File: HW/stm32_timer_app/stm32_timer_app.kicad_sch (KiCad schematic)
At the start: 20 parts, among them J1 105164-0001, J2 61300411121, Q1 BTA10-600BRG, U1 RT9193-33GB, U2 MOC3041SM, U3 STM32F103C8T6

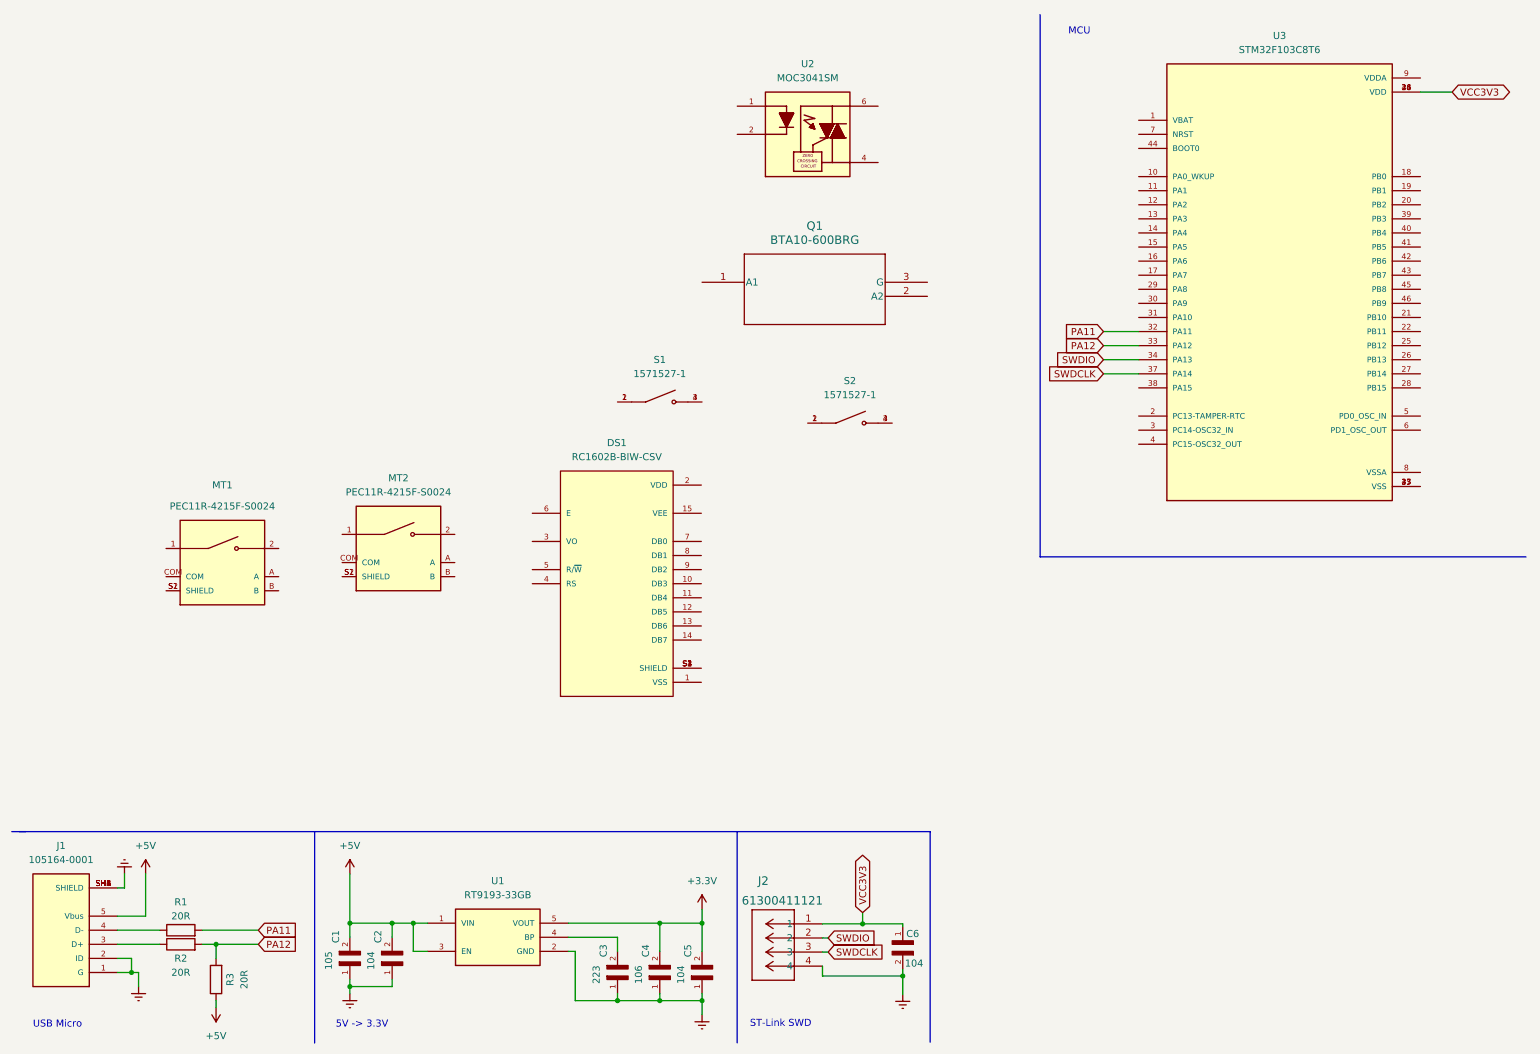
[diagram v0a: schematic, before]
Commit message: schematic design
added schematic for 3v3 regulator, reset switch, micro USB and two led
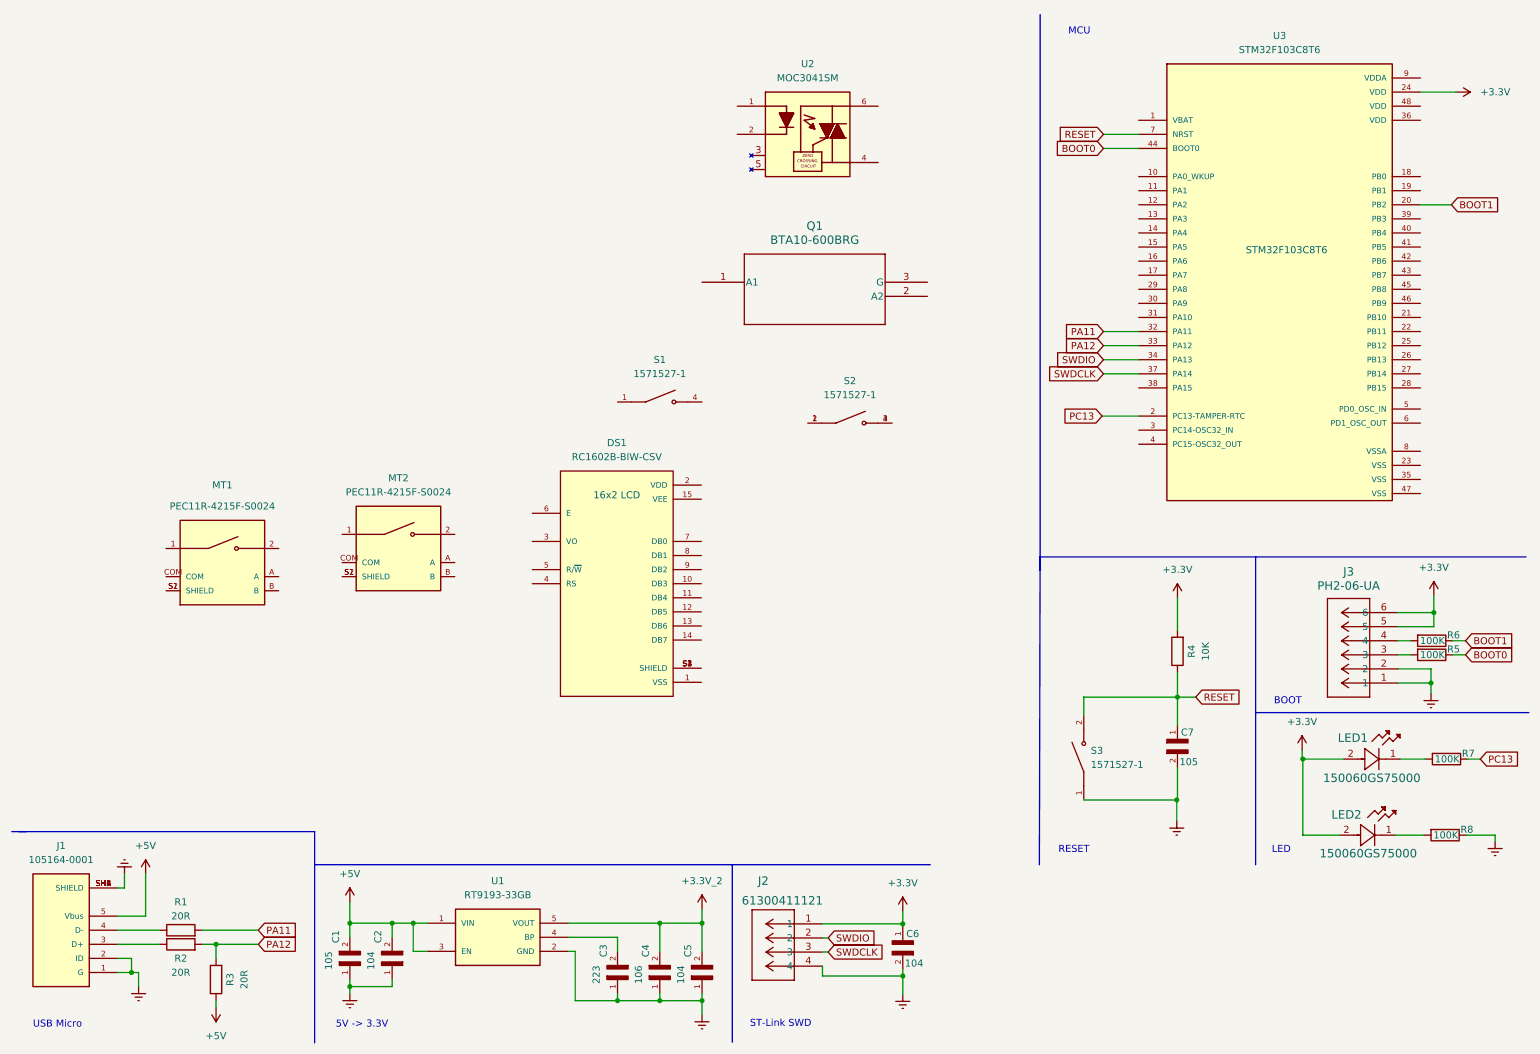
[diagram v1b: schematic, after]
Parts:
- added C7: 105, LD03ZD475MAB2A:CAPC1608X90, symbol LD03ZD475MAB2A:LD03ZD475MAB2A
- added J3: PH2-06-UA, PH2_06_UA:CONN_PH2-06-UA_ADM, symbol CONN_PH2:PH2-06-UA
- added LED1, LED2: 150060GS75000, LED_150060GS75000_WRE, symbol 150060GS75000:150060GS75000
- added R4: 10K, Resistor_SMD:R_0603_1608Metric, symbol Device:R
- added R5, R6, R7, R8: 100K, Resistor_SMD:R_0603_1608Metric, symbol Device:R
- added S3: 1571527-1, 1571527-1:SW_1571527-1, symbol 1571527-1:1571527-1
- DS1: Package None -> 16x2 LCD
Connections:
- net PC13: now reaches U3.2 (PC13-TAMPER-RTC)
- net PC13: now also R7.1
- net BOOT1: now reaches U3.20 (PB2)
- net BOOT1: now also R6.1
- net BOOT0: now reaches U3.44 (BOOT0)
- net BOOT0: now also R5.1
- net RESET: now reaches U3.7 (NRST)
- net RESET: now also C7.1, R4.1, S3.2, S3.4
- net +3.3V: no longer names the net of C4.2, C5.2, U1.5 (VOUT)
- net +5V: no longer names the net of C1.2, C2.2, U1.1 (VIN), U1.3 (EN)
- net +5V: no longer J1.5 (Vbus), R3.1
- removed net GNDREF: C1.1, C2.1, C3.1, C4.1, C5.1, C6.2, J1.1 (G), J1.2 (ID), J1.SH1 (SHIELD), J1.SH2 (SHIELD), J1.SH3 (SHIELD), J1.SH4 (SHIELD), J1.SH5 (SHIELD), J1.SH6 (SHIELD), J2.4, U1.2 (GND)
- removed net VCC3V3: C6.1, J2.1, U3.24 (VDD), U3.36 (VDD), U3.48 (VDD)
- new net: C3.1, C4.1, C5.1, U1.2 (GND)
- new net: J1.1 (G), J1.2 (ID)
- new net: J1.SH1 (SHIELD), J1.SH2 (SHIELD), J1.SH3 (SHIELD), J1.SH4 (SHIELD), J1.SH5 (SHIELD), J1.SH6 (SHIELD)
- new net: C6.1, J2.1
- new net: C6.2, J2.4
- new net: C1.1, C2.1
- new net: LED2.1, R8.2
- new net: LED1.2, LED2.2
- new net: J3.1, J3.2
- new net: J3.3, R5.2
- new net: J3.4, R6.2
- new net: J3.5, J3.6
- new net: LED1.1, R7.2
- new net: C7.2, S3.1, S3.3
- now unconnected: U3.23 (VSS), U3.35 (VSS), U3.47 (VSS)
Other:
- note added: "BOOT"
- note added: "LED"
- note added: "RESET"

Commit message: schematic design
schematic design revision 1
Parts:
- added C10, C11, C8, C9: 104, LD03ZD475MAB2A:CAPC1608X90, symbol LD03ZD475MAB2A:LD03ZD475MAB2A
- added C12, C13, C14, C15: 20p, LD03ZD475MAB2A:CAPC1608X90, symbol LD03ZD475MAB2A:LD03ZD475MAB2A
- added C16: ECW-FD2J273KQ, CAP_ECWFD_FORMINGQ_12.6LX06.9TX09.9H_PAN, symbol ECW_FD2J273KQ:ECW-FD2J273KQ
- added CR1, CR2, CR3, CR4, CR5, CR6: 1N4148W-13-F, SOD123_DIO, symbol 1N4148W_13_F:1N4148W-13-F
- added J4, J5: 691213710002, 691213710002:691213710002, symbol 691213710002:691213710002
- added R10, R11, R12, R13, R14, R15, R16, R17, R18, R19, R20, R21: 10K, Resistor_SMD:R_0603_1608Metric, symbol Device:R
- added R22: TC33X-2-102E, TC33X_2_102E:TRIM_TC33X-2-102E, symbol TC33X-2-102E:TC33X-2-102E
- added R23, R24: 220, Resistor_SMD:R_0603_1608Metric, symbol Device:R
- added R25: 1K, Resistor_SMD:R_0603_1608Metric, symbol Device:R
- added R26: 360, Resistor_SMD:R_0603_1608Metric, symbol Device:R
- added R27: 330, Resistor_SMD:R_0603_1608Metric, symbol Device:R
- added R29: 39, RES_OY_OHM, symbol OY390KE:OY390KE
- added R9: 20R, Resistor_SMD:R_0603_1608Metric, symbol Device:R
- added Y1: ABL-8.000MHZ-B2, ABL-8.000MHZ-B2:XTAL_HC49P488W46L1150T500H350, symbol ABL-8.000MHZ-B2:ABL-8.000MHZ-B2
- added Y2: ABS25-32.768KHZ-6-4-T, ABS25-32.768KHZ-6-4-T:XTAL_ABS25-32.768KHZ-6-4-T, symbol ABS25-32.768KHZ-6-4-T:ABS25-32.768KHZ-6-4-T
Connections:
- net +3.3V: now reaches R4.2
- net +3.3V: now also C4.2, C5.2, C6.1, J2.1, J3.5, J3.6, LED1.2, LED2.2, S1.3, S1.4, S2.3, S2.4, U1.5 (VOUT), U3.13 (PA3), U3.14 (PA4), U3.24 (VDD), U3.36 (VDD), U3.48 (VDD), C10.2, C11.2, C8.2, C9.2, R16.2, R17.2, R18.2, R19.2, R20.2, R21.2
- net at DS1.10 (DB3): now also DS1.16 (K), DS1.7 (DB0), DS1.8 (DB1), DS1.9 (DB2)
- net PB3: now reaches DS1.11 (DB4)
- net PB3: now also U3.39 (PB3)
- net PB4: now reaches DS1.12 (DB5)
- net PB4: now also U3.40 (PB4)
- net PB5: now reaches DS1.13 (DB6)
- net PB5: now also U3.41 (PB5)
- net PB6: now reaches DS1.14 (DB7)
- net PB6: now also U3.42 (PB6)
- net +5V: now reaches DS1.15 (A)
- net +5V: now also C1.2, C2.2, DS1.2 (VDD), J1.5 (Vbus), R3.1, U1.1 (VIN), U1.3 (EN), R22.1
- net at DS1.3 (VO): now also R22.2
- net PB1: now reaches DS1.4 (RS)
- net PB1: now also U3.19 (PB1)
- net at DS1.5 (R/~{W}): now also R22.3
- net PB0: now reaches DS1.6 (E)
- net PB0: now also U3.18 (PB0)
- net at U2.1: now also R25.2
- net at U2.4: now also Q1.3 (G), R27.2
- net at U2.6: now also R26.1
- net at S1.1, S1.2: now also R23.2
- net at MT2.1: now also MT2.COM, MT2.S1 (SHIELD), MT2.S2 (SHIELD)
- net at MT2.2: now also CR4.2, R14.1, R19.1
- net at MT2.A: now also CR5.2, R13.1, R20.1
- net at MT2.B: now also CR6.2, R15.1, R21.1
- net at Q1.1 (A1): now also J4.1, R26.2, R29.2
- net at Q1.2 (A2): now also C16.1, J5.2, R27.1
- net PA0: now reaches U3.10 (PA0_WKUP)
- net PA0: now also CR5.1, R13.2
- net PA1: now reaches U3.11 (PA1)
- net PA1: now also CR6.1, R15.2
- net PA2: now reaches U3.12 (PA2)
- net PA2: now also CR4.1, R14.2
- net PA5: now reaches U3.15 (PA5)
- net PA5: now also CR1.1, R10.2
- net PA6: now reaches U3.16 (PA6)
- net PA6: now also CR2.1, R11.2
- net PA7: now reaches U3.17 (PA7)
- net PA7: now also CR3.1, R12.2
- net PC14: now reaches U3.3 (PC14-OSC32_IN)
- net PC14: now also C14.2, Y2.1
- net PC15: now reaches U3.4 (PC15-OSC32_OUT)
- net PC15: now also C15.2, Y2.4
- net PB7: now reaches U3.43 (PB7)
- net PB7: now also R25.1
- net OSCIN: now reaches U3.5 (PD0_OSC_IN)
- net OSCIN: now also C12.2, R9.1, Y1.1
- net OSCOUT: now reaches U3.6 (PD1_OSC_OUT)
- net OSCOUT: now also C13.2, R9.2, Y1.2
- net at S2.1, S2.2: now also R24.2
- net at MT1.1: now also MT1.COM, MT1.S1 (SHIELD), MT1.S2 (SHIELD)
- net at MT1.2: now also CR1.2, R10.1, R16.1
- net at MT1.A: now also CR2.2, R11.1, R17.1
- net at MT1.B: now also CR3.2, R12.1, R18.1
- new net: J4.2, J5.1
- new net: C14.1, C15.1
- new net: C10.1, C11.1, C8.1, C9.1
- new net: C16.2, R29.1
- new net: C12.1, C13.1
- new net: Y2.2 (NC), Y2.3 (NC)
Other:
- note added: "16x2 LCD"
- note added: "AC in"
- note added: "Rotatory Encoder"
- note added: "SWITCH"
- note added: "TRIAC DRIVE"
- note added: "load"
- note added: "neutral"
- moved on the sheet: MT1, Q1, S1, U2, U3

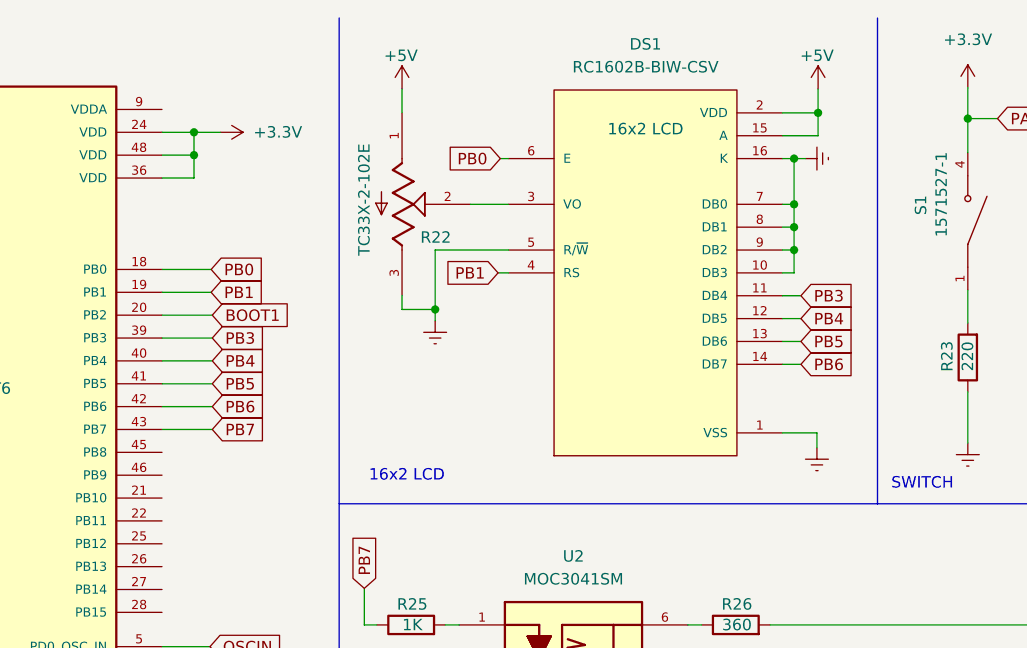
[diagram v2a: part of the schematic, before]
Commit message: replace 16x2 lcd with 2.4" OLED foot print
replace 16x2 lcd with 2.4" OLED foot print
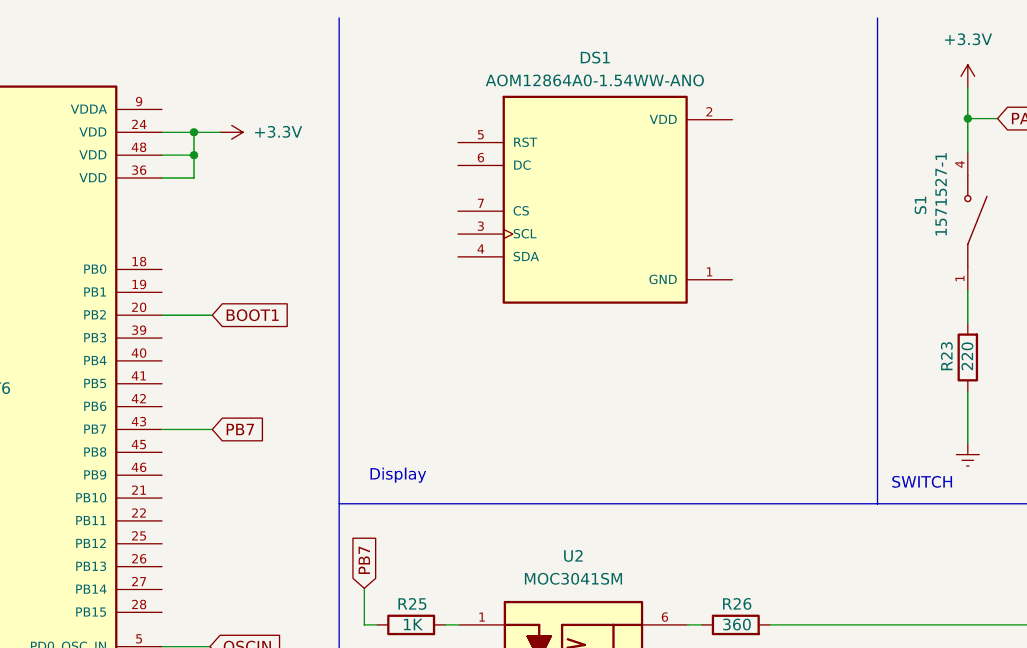
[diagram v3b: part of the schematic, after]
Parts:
- removed DS1: RC1602B-BIW-CSV, RC1602B-BIW-CSV:LCD_RC1602B-BIW-CSV, symbol RC1602B-BIW-CSV:RC1602B-BIW-CSV
- removed R22: TC33X-2-102E, TC33X_2_102E:TRIM_TC33X-2-102E, symbol TC33X-2-102E:TC33X-2-102E
- added DS1: AOM12864A0-1.54WW-ANO, AOM12864A0-1.54WW-ANO:LCD_AOM12864A0-1.54WW-ANO, symbol AOM12864A0-1.54WW-ANO:AOM12864A0-1.54WW-ANO
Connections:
- net PB0: no longer names the net of U3.18 (PB0)
- net PB1: no longer names the net of U3.19 (PB1)
- net PB3: no longer names the net of U3.39 (PB3)
- net PB4: no longer names the net of U3.40 (PB4)
- net PB5: no longer names the net of U3.41 (PB5)
- net PB6: no longer names the net of U3.42 (PB6)
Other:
- note added: "Display"
- note removed: "16x2 LCD"
